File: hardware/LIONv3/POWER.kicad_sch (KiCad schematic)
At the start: 28 parts, among them U10 INA226AIDGSR, U11 TPS259474ARPWR, U12 XL-1608UGC-04, U13 XL-1608SURC-06, U16 HC-1_25-2PWT, U17 HC-1_25-2PWT, U18 HC-1_25-2PWT, U20 TLV76733DRVR

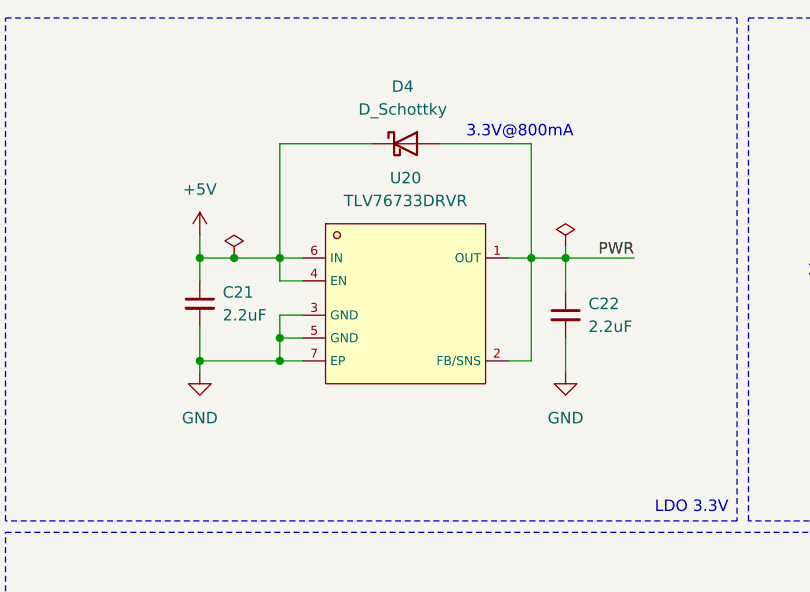
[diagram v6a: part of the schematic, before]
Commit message: feat(hardware): change SPI terminology (new OSHWA naming conventions)
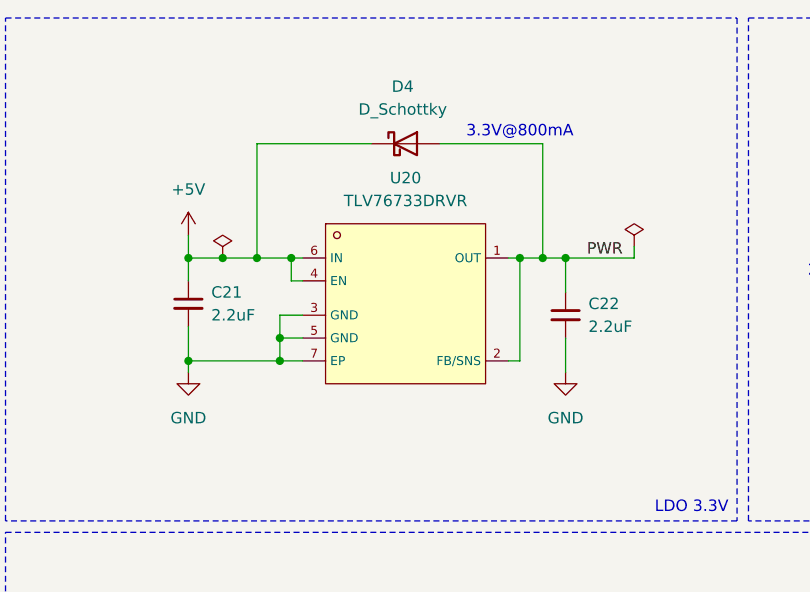
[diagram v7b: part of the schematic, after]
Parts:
- FB2: footprint Capacitor_SMD:C_0805_2012Metric -> Inductor_SMD:L_0805_2012Metric
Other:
- moved on the sheet: C21

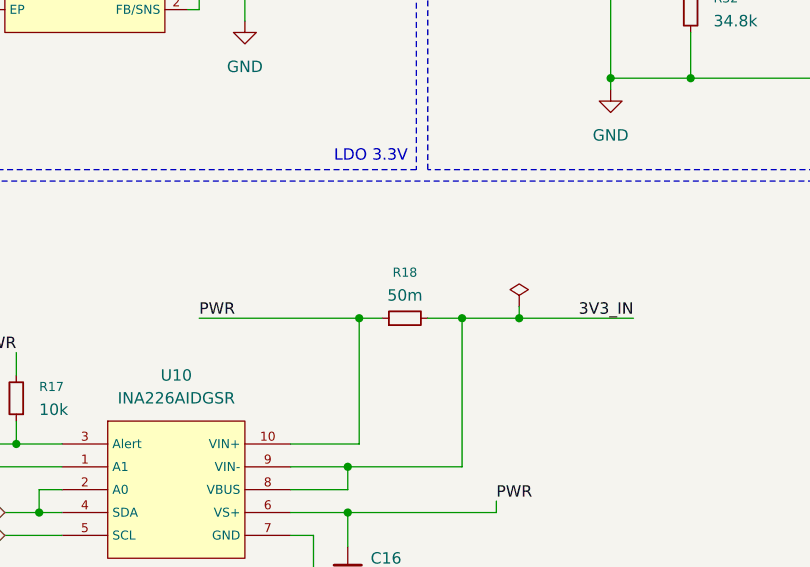
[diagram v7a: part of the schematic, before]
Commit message: feat(hardware): add shunt resistor rating to schematic
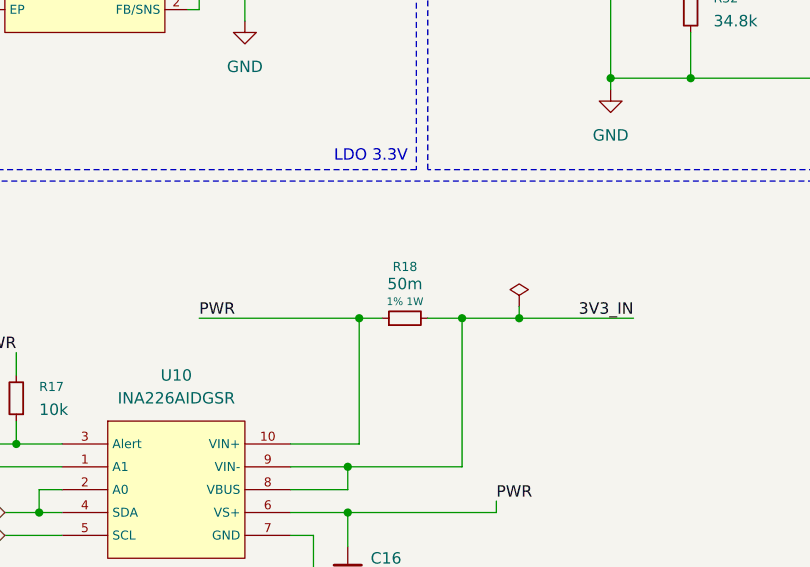
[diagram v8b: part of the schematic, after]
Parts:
- R18: Rated_Power (none) -> 1W; Rating (none) -> ${Tolerance} ${Rated_Power}; Tolerance (none) -> 1%
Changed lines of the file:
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@@
 		(in_pos_files yes)
 		(dnp no)
-		(fields_autoplaced yes)
 		(property "Reference" "R18"
-			(at 93.98 81.28 90)
+			(at 93.9892 80.6441 90)
 			(show_name no)
 			(do_not_autoplace no)
@@
 		)
 		(property "Value" "50m"
-			(at 93.98 83.82 90)
+			(at 93.98 82.55 90)
 			(show_name no)
 			(do_not_autoplace no)
@@
 				)
 			)
+		)
+		(property "Tolerance" "1%"
+			(at 93.98 86.36 90)
+			(hide yes)
+			(show_name no)
+			(do_not_autoplace no)
+			(effects
+				(font
+					(size 1.27 1.27)
+				)
+			)
+		)
+		(property "Rated_Power" "1W"
+			(at 93.98 86.36 90)
+			(hide yes)
+			(show_name no)
+			(do_not_autoplace no)
+			(effects
+				(font
+					(size 1.27 1.27)
+				)
+			)
+		)
+		(property "Rating" "${Tolerance} ${Rated_Power}"
+			(at 93.9892 84.5077 90)
+			(show_name no)
+			(do_not_autoplace no)
+			(effects
+				(font
+					(size 0.8467 0.8467)
+				)
+			)
